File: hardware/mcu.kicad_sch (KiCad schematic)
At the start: 22 parts, among them J6 Micro_SD_Card_Det1, SW24 BOOT, SW8 RST, U1 ESP32-S3-WROOM-1

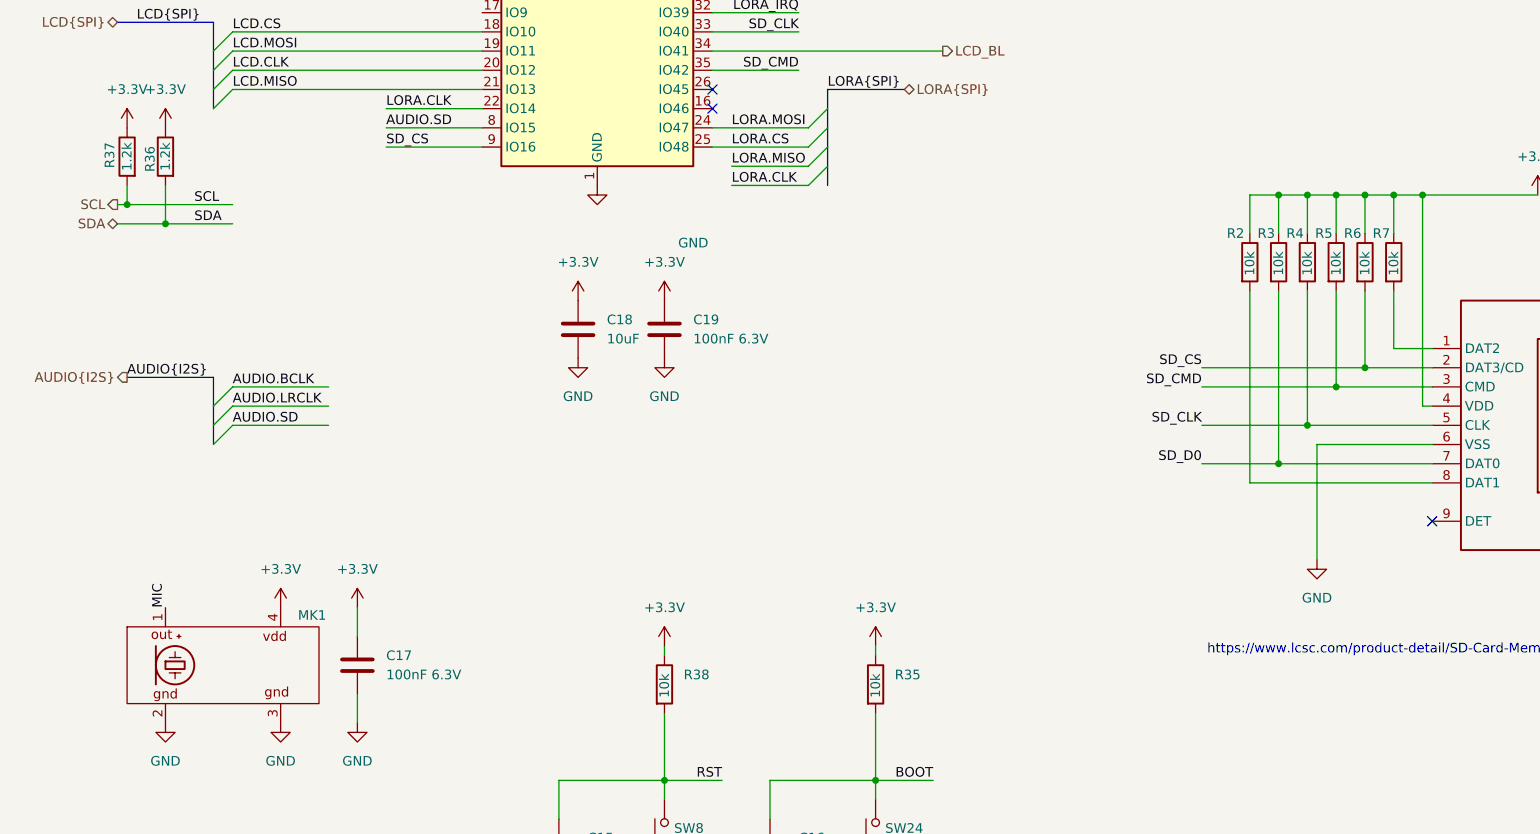
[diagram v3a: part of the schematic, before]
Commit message: Associate all LCSC component
Change sdcard pullup resistor to 47K
Center main schematic
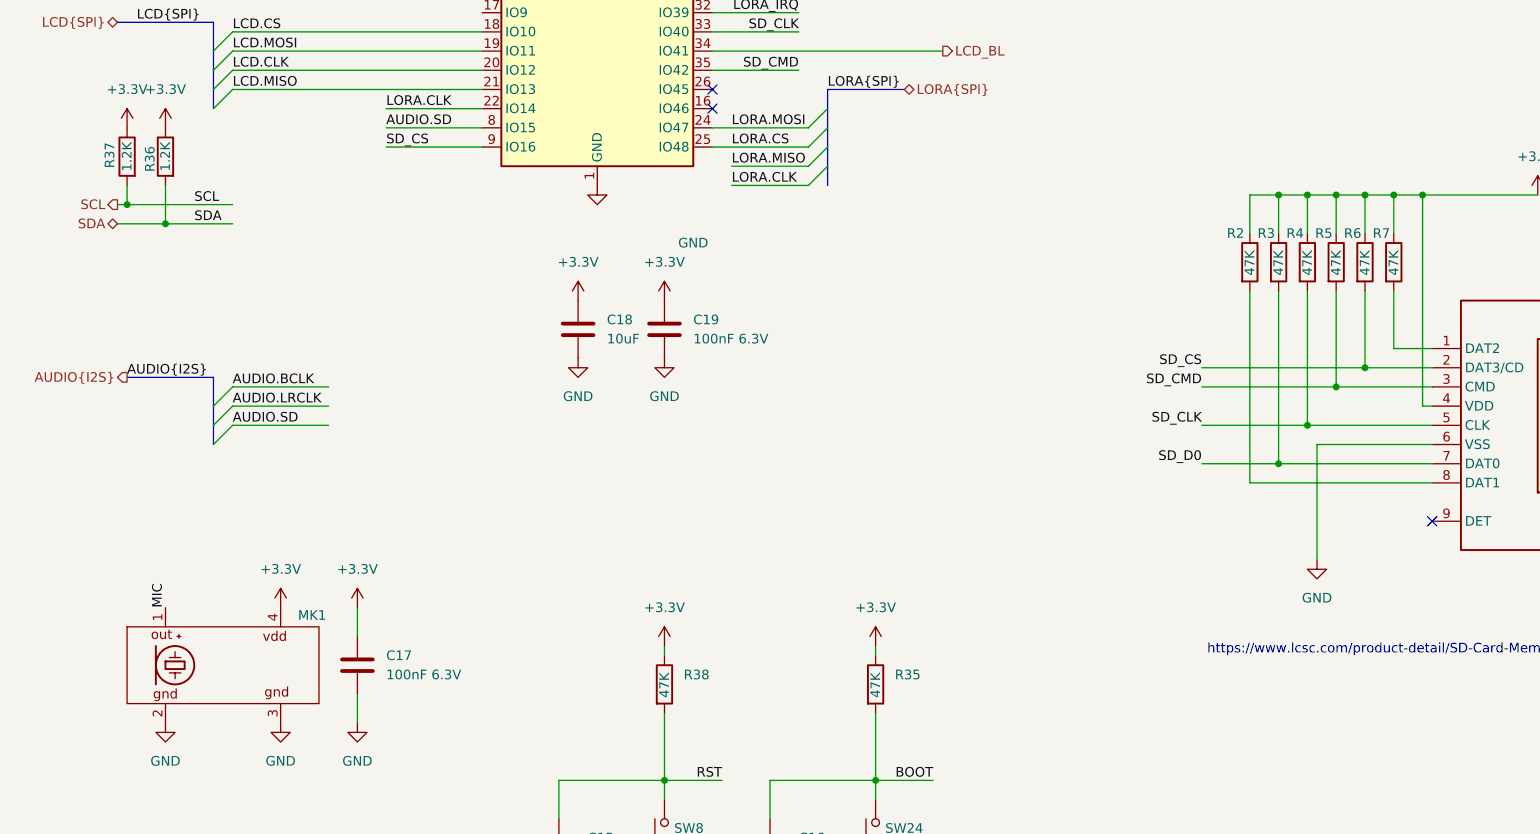
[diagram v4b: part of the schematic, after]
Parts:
- C15, C16, C18: LCSC (none) -> C1691
- R2: value 10k -> 47K; LCSC TODO -> C105579
- R3, R35, R38, R4, R5, R6, R7: value 10k -> 47K; LCSC (none) -> C105579
- R36, R37: value 1.2k -> 1.2K; LCSC (none) -> C114605
- SW24, SW8: LCSC (none) -> C2888430
- U1: LCSC (none) -> C2913201
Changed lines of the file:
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@@
+			)
+		)
+		(property "LCSC" "C2888430"
+			(at 123.19 180.34 0)
+			(effects
+				(font
+					(size 1.27 1.27)
+				)
+				(hide yes)
 			)
 		)
@@
 			)
 		)
-		(property "Value" "10k"
+		(property "Value" "47K"
 			(at 172.72 105.918 90)
 			(effects
@@
 			)
 		)
-		(property "LCSC" "TODO"
+		(property "LCSC" "C105579"
 			(at 172.72 104.14 0)
 			(effects
@@
 			)
 		)
-		(property "Value" "1.2k"
+		(property "Value" "1.2K"
 			(at 29.21 90.17 90)
 			(effects
@@
 			)
 		)
+		(property "LCSC" "C114605"
+			(at 29.21 90.17 0)
+			(effects
+				(font
+					(size 1.27 1.27)
+				)
+				(hide yes)
+			)
+		)
 		(pin "2"
 		)
@@
 			)
 		)
-		(property "Value" "10k"
+		(property "Value" "47K"
 			(at 95.25 161.798 90)
 			(effects
@@
 		)
 		(property "Description" "Resistor"
+			(at 95.25 160.02 0)
+			(effects
+				(font
+					(size 1.27 1.27)
+				)
+				(hide yes)
+			)
+		)
+		(property "LCSC" "C105579"
 			(at 95.25 160.02 0)
 			(effects
@@
 			)
 		)
-		(property "Value" "1.2k"
+		(property "Value" "1.2K"
 			(at 24.13 90.17 90)
 			(effects
@@
 		)
 		(property "Description" "Resistor"
+			(at 24.13 90.17 0)
+			(effects
+				(font
+					(size 1.27 1.27)
+				)
+				(hide yes)
+			)
+		)
+		(property "LCSC" "C114605"
 			(at 24.13 90.17 0)
 			(effects
@@
 			)
 		)
+		(property "LCSC" "C2888430"
+			(at 95.25 180.34 0)
+			(effects
+				(font
+					(size 1.27 1.27)
+				)
+				(hide yes)
+			)
+		)
 		(pin "1"
 		)
@@
 			)
 		)
-		(property "Value" "10k"
+		(property "Value" "47K"
 			(at 176.53 105.918 90)
 			(effects
@@
 			)
 		)
+		(property "LCSC" "C105579"
+			(at 176.53 104.14 0)
+			(effects
+				(font
+					(size 1.27 1.27)
+				)
+				(hide yes)
+			)
+		)
 		(pin "2"
 		)
@@
 			)
 		)
+		(property "LCSC" "C2913201"
+			(at 86.36 66.04 0)
+			(effects
+				(font
+					(size 1.27 1.27)
+				)
+				(hide yes)
+			)
+		)
 		(pin "6"
 		)
@@
 			)
 		)
+		(property "LCSC" "C1691"
+			(at 83.82 113.03 0)
+			(effects
+				(font
+					(size 1.27 1.27)
+				)
+				(hide yes)
+			)
+		)
 		(pin "2"
 		)
@@
 			)
 		)
-		(property "Value" "10k"
+		(property "Value" "47K"
 			(at 191.77 105.918 90)
 			(effects
@@
 			)
 		)
+		(property "LCSC" "C105579"
+			(at 191.77 104.14 0)
+			(effects
+				(font
+					(size 1.27 1.27)
+				)
+				(hide yes)
+			)
+		)
 		(pin "2"
 		)
@@
 			)
 		)
-		(property "Value" "10k"
+		(property "Value" "47K"
 			(at 187.96 105.918 90)
 			(effects
@@
 			)
 		)
+		(property "LCSC" "C105579"
+			(at 187.96 104.14 0)
+			(effects
+				(font
+					(size 1.27 1.27)
+				)
+				(hide yes)
+			)
+		)
 		(pin "2"
 		)
@@
 			)
 		)
+		(property "LCSC" "C1691"
+			(at 109.22 181.61 0)
+			(effects
+				(font
+					(size 1.27 1.27)
+				)
+				(hide yes)
+			)
+		)
 		(pin "2"
 		)
@@
 			)
 		)
-		(property "Value" "10k"
+		(property "Value" "47K"
 			(at 123.19 161.798 90)
 			(effects
@@
 		)
 		(property "Description" "Resistor"
+			(at 123.19 160.02 0)
+			(effects
+				(font
+					(size 1.27 1.27)
+				)
+				(hide yes)
+			)
+		)
+		(property "LCSC" "C105579"
 			(at 123.19 160.02 0)
 			(effects
@@
 			)
 		)
+		(property "LCSC" "C1691"
+			(at 81.28 181.61 0)
+			(effects
+				(font
+					(size 1.27 1.27)
+				)
+				(hide yes)
+			)
+		)
 		(pin "2"
 		)
@@
 			)
 		)
-		(property "Value" "10k"
+		(property "Value" "47K"
 			(at 180.34 105.918 90)
 			(effects
@@
 			)
 		)
+		(property "LCSC" "C105579"
+			(at 180.34 104.14 0)
+			(effects
+				(font
+					(size 1.27 1.27)
+				)
+				(hide yes)
+			)
+		)
 		(pin "2"
 		)
@@
 			)
 		)
-		(property "Value" "10k"
+		(property "Value" "47K"
 			(at 184.15 105.918 90)
 			(effects
@@
 			(at 184.15 104.14 0)
 			(effects
+				(font
+					(size 1.27 1.27)
+				)
+				(hide yes)
+			)
+		)
+		(property "LCSC" "C105579"
+			(at 184.15 104.14 0)
+			(effects

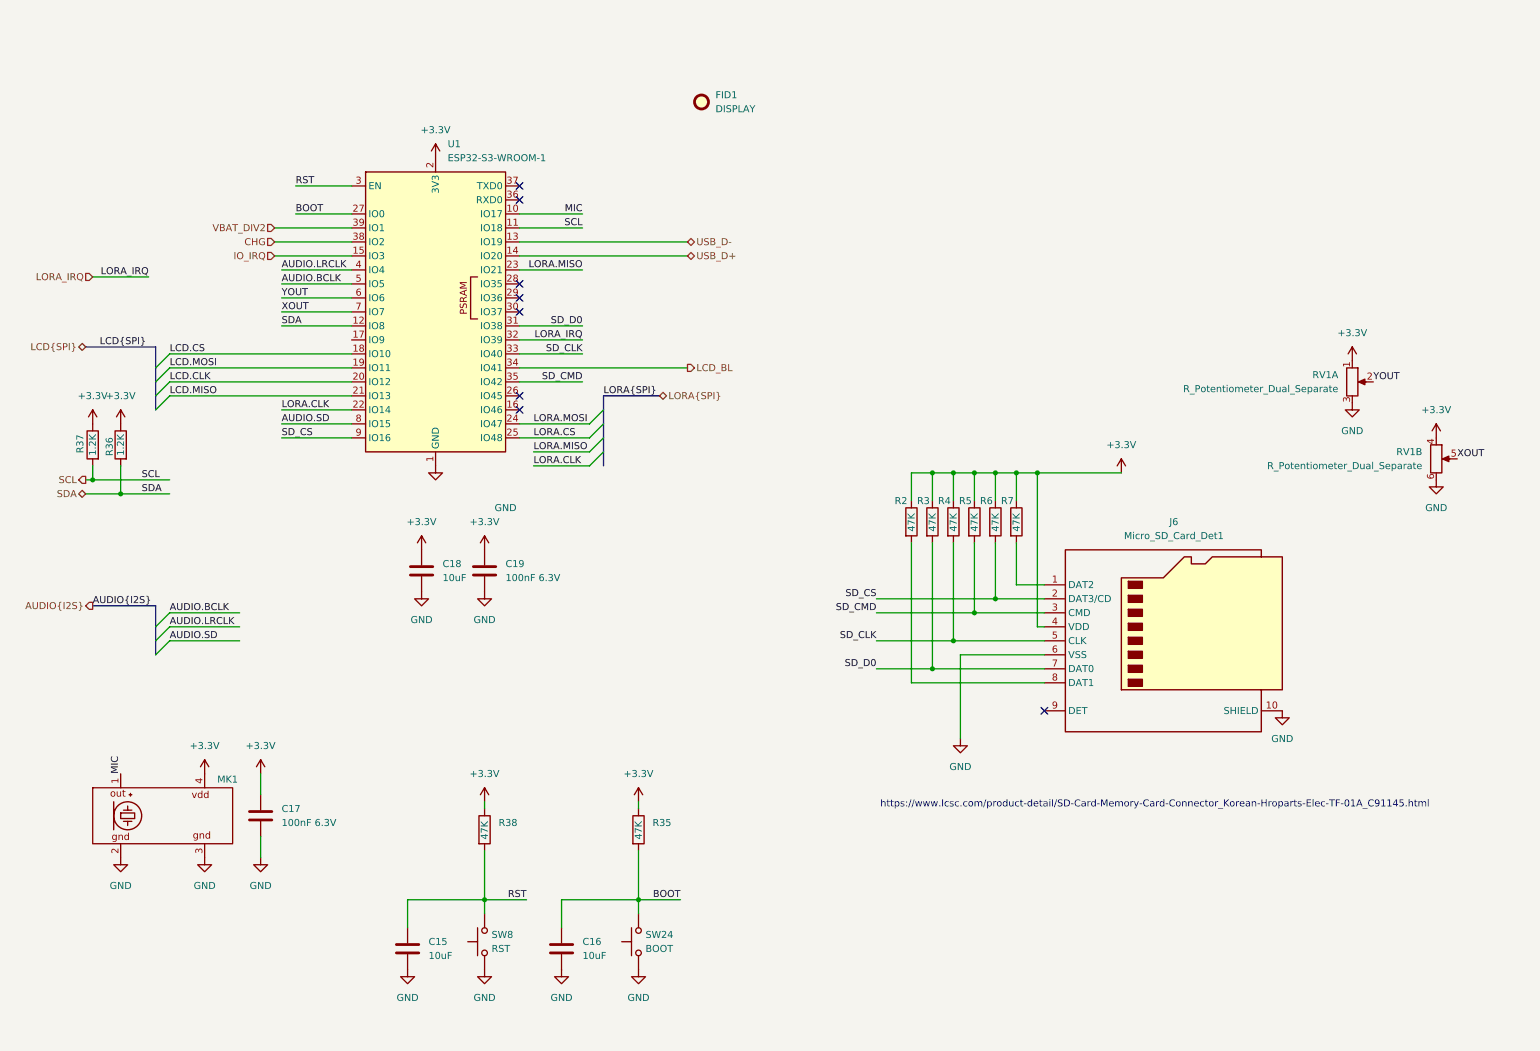
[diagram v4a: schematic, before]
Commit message: Beautified schematic, added I2C addresses
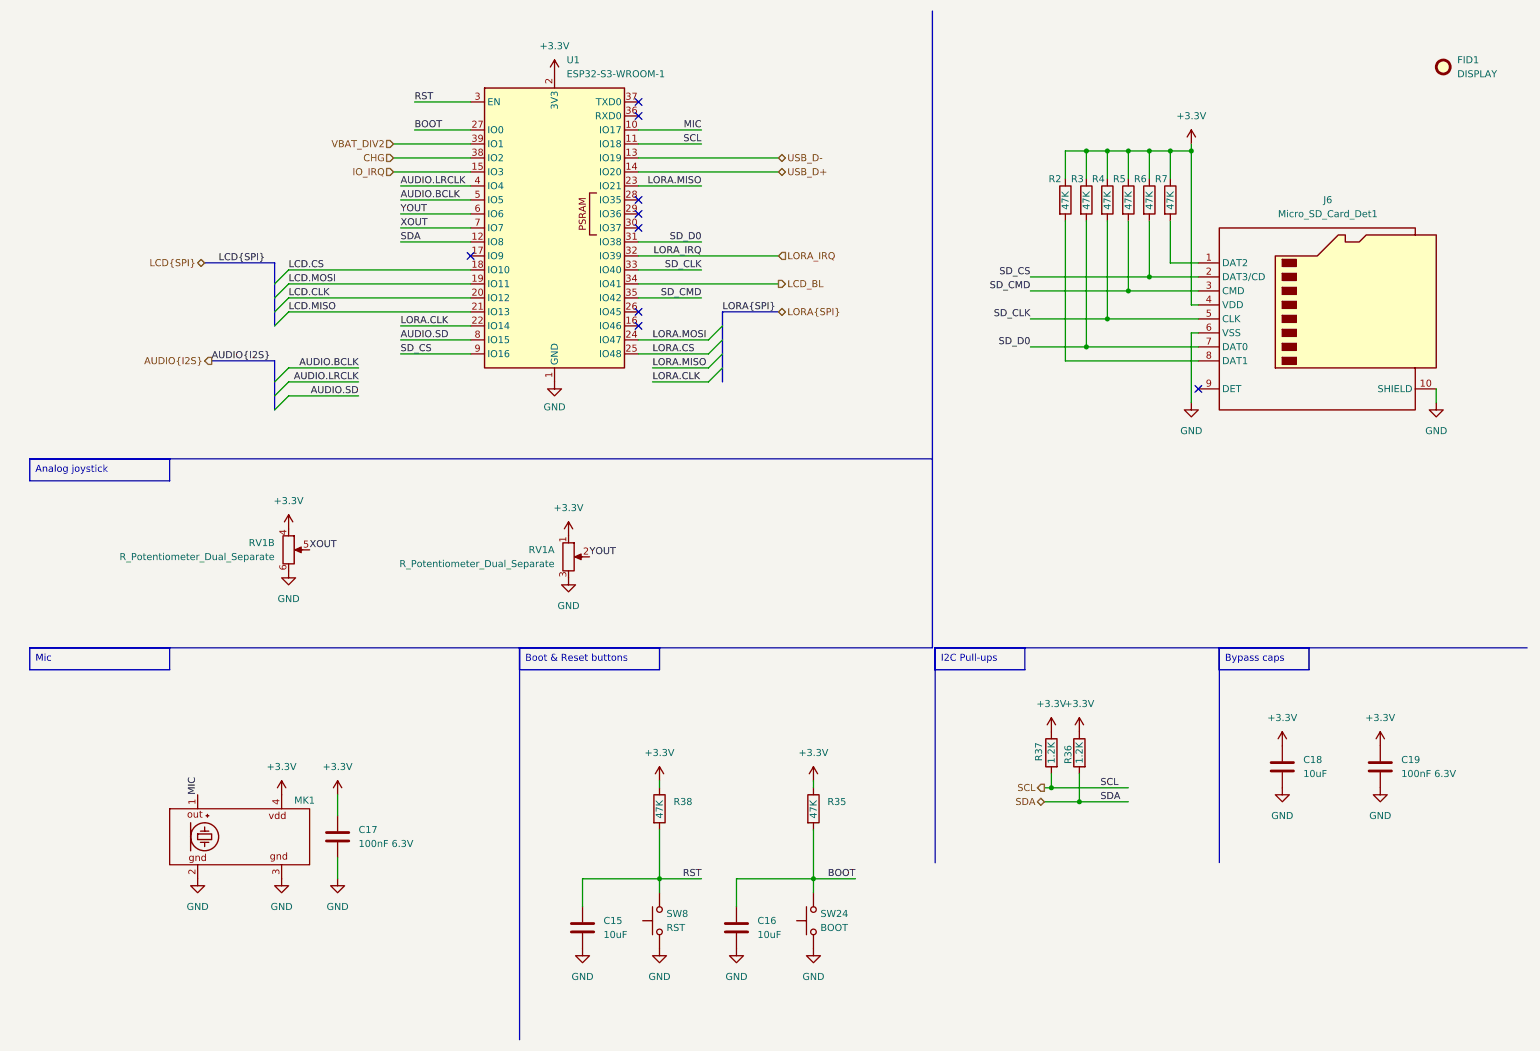
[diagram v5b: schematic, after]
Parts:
- J6: LCSC Link (none) -> https://www.lcsc.com/product-detail/SD-Card-Memory-Card-Con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
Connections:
- no-connect marks 8 -> 9
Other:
- note removed: "https://www.lcsc.com/product-detail/SD-Card-Memory-Card-Connector_Korean-Hroparts-Elec-TF-01A_C91145.html"
- moved on the sheet: C15, C16, C17, C18, C19, FID1, J6, MK1, R2, R3, R35, R36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

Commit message: Fix rotation and position offset of components
Fix lora module rotation
Fix esp32 module position offset
Fix sd card position offset
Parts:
- J6: JLCPCB Position Offset (none) -> 0,5.5
- U1: JLCPCB Position Offset (none) -> 0,-3.65
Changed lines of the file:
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@@
 			)
 		)
+		(property "JLCPCB Position Offset" ""
+			(at 154.94 176.53 0)
+			(effects
+				(font
+					(size 1.27 1.27)
+				)
+				(hide yes)
+			)
+		)
 		(pin "1"
 		)
@@
 			)
 		)
+		(property "JLCPCB Position Offset" ""
+			(at 200.66 45.72 0)
+			(effects
+				(font
+					(size 1.27 1.27)
+				)
+				(hide yes)
+			)
+		)
 		(pin "2"
 		)
@@
 			)
 		)
+		(property "JLCPCB Position Offset" ""
+			(at 203.2 146.05 0)
+			(effects
+				(font
+					(size 1.27 1.27)
+				)
+				(hide yes)
+			)
+		)
 		(pin "2"
 		)
@@
 			)
 		)
+		(property "JLCPCB Position Offset" ""
+			(at 127 156.21 0)
+			(effects
+				(font
+					(size 1.27 1.27)
+				)
+				(hide yes)
+			)
+		)
 		(pin "1"
 		)
@@
 			)
 		)
+		(property "JLCPCB Position Offset" ""
+			(at 198.12 146.05 0)
+			(effects
+				(font
+					(size 1.27 1.27)
+				)
+				(hide yes)
+			)
+		)
 		(pin "2"
 		)
@@
 			)
 		)
+		(property "JLCPCB Position Offset" ""
+			(at 269.24 21.59 0)
+			(effects
+				(font
+					(size 1.27 1.27)
+				)
+				(hide yes)
+			)
+		)
 		(instances
 			(project "badge"
@@
 			)
 		)
+		(property "JLCPCB Position Offset" ""
+			(at 127 176.53 0)
+			(effects
+				(font
+					(size 1.27 1.27)
+				)
+				(hide yes)
+			)
+		)
 		(pin "1"
 		)
@@
 			)
 		)
+		(property "JLCPCB Position Offset" ""
+			(at 204.47 45.72 0)
+			(effects
+				(font
+					(size 1.27 1.27)
+				)
+				(hide yes)
+			)
+		)
 		(pin "2"
 		)
@@
 			)
 		)
+		(property "JLCPCB Position Offset" ""
+			(at 49.53 161.29 0)
+			(effects
+				(font
+					(size 1.27 1.27)
+				)
+				(hide yes)
+			)
+		)
 		(pin "2"
 		)
@@
 			)
 		)
+		(property "JLCPCB Position Offset" "0,-3.65"
+			(at 107.95 50.8 0)
+			(effects
+				(font
+					(size 1.27 1.27)
+				)
+				(hide yes)
+			)
+		)
 		(pin "6"
 		)
@@
 			)
 		)
+		(property "JLCPCB Position Offset" ""
+			(at 240.03 148.59 0)
+			(effects
+				(font
+					(size 1.27 1.27)
+				)
+				(hide yes)
+			)
+		)
 		(pin "2"
 		)
@@
 			)
 		)
+		(property "JLCPCB Position Offset" ""
+			(at 219.71 45.72 0)
+			(effects
+				(font
+					(size 1.27 1.27)
+				)
+				(hide yes)
+			)
+		)
 		(pin "2"
 		)
@@
 			)
 		)
+		(property "JLCPCB Position Offset" ""
+			(at 215.9 45.72 0)
+			(effects
+				(font
+					(size 1.27 1.27)
+				)
+				(hide yes)
+			)
+		)
 		(pin "2"
 		)
@@
 			)
 		)
+		(property "JLCPCB Position Offset" ""
+			(at 140.97 177.8 0)
+			(effects
+				(font
+					(size 1.27 1.27)
+				)
+				(hide yes)
+			)
+		)
 		(pin "2"
 		)
@@
 			)
 		)
+		(property "JLCPCB Position Offset" "0,5.5"
+			(at 247.65 67.31 0)
+			(effects
+				(font
+					(size 1.27 1.27)
+				)
+				(hide yes)
+			)
+		)
 		(pin "6"
 		)
@@
 			)
 		)
+		(property "JLCPCB Position Offset" ""
+			(at 154.94 156.21 0)
+			(effects
+				(font
+					(size 1.27 1.27)
+				)
+				(hide yes)
+			)
+		)
 		(pin "1"
 		)
@@
 			)
 		)
+		(property "JLCPCB Position Offset" ""
+			(at 257.81 148.59 0)
+			(effects
+				(font
+					(size 1.27 1.27)
+				)
+				(hide yes)
+			)
+		)
 		(pin "2"
 		)
@@
 			)
 		)
+		(property "JLCPCB Position Offset" ""
+			(at 113.03 177.8 0)
+			(effects
+				(font
+					(size 1.27 1.27)
+				)
+				(hide yes)
+			)
+		)
 		(pin "2"
 		)
@@
 			)
 		)
+		(property "JLCPCB Position Offset" ""
+			(at 208.28 45.72 0)
+			(effects
+				(font
+					(size 1.27 1.27)
+				)
+				(hide yes)
+			)
+		)
 		(pin "2"
 		)
@@
 			)
 		)
+		(property "JLCPCB Position Offset" ""
+			(at 212.09 45.72 0)
+			(effects
+				(font
+					(size 1.27 1.27)
+				)
+				(hide yes)
+			)
+		)
 		(pin "2"
 		)
@@
 			)
 		)
+		(property "JLCPCB Position Offset" ""
+			(at 110.49 110.49 0)
+			(effects
+				(font
+					(size 1.27 1.27)
+				)
+				(hide yes)
+			)
+		)
 		(pin "2"
 		)
@@
 			)
 		)
+		(property "JLCPCB Position Offset" ""
+			(at 59.69 109.22 0)
+			(effects
+				(font
+					(size 1.27 1.27)
+				)
+				(hide yes)
+			)
+		)
 		(pin "2"
 		)
@@
 			(at 68.58 161.29 0)
 			(effects
+				(font
+					(size 1.27 1.27)
+				)
+				(hide yes)
+			)
+		)
+		(property "JLCPCB Position Offset" ""
+			(at 68.58 161.29 0)
+			(effects

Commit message: add joystick lcsc code, for real
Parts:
- RV1: LCSC (none) -> C17511761
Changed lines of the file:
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@@
+			)
+		)
+		(property "LCSC" "C17511761"
+			(at 110.49 110.49 0)
+			(effects
+				(font
+					(size 1.27 1.27)
+				)
+				(hide yes)
 			)
 		)
@@
 			(at 59.69 109.22 0)
 			(effects
+				(font
+					(size 1.27 1.27)
+				)
+				(hide yes)
+			)
+		)
+		(property "LCSC" "C17511761"
+			(at 59.69 109.22 0)
+			(effects

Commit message: update lcsc codes to use (new?) basic components
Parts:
- C15, C16, C18: LCSC C1691 -> C19702
- R2, R3, R35, R38, R4, R5, R6, R7: LCSC C105579 -> C25819
- R36, R37: LCSC C114605 -> C22765
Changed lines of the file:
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@@
 			)
 		)
-		(property "LCSC" "C105579"
+		(property "LCSC" "C25819"
 			(at 200.66 45.72 0)
 			(effects
@@
 			)
 		)
-		(property "LCSC" "C114605"
+		(property "LCSC" "C22765"
 			(at 203.2 146.05 0)
 			(effects
@@
 			)
 		)
-		(property "LCSC" "C105579"
+		(property "LCSC" "C25819"
 			(at 127 156.21 0)
 			(effects
@@
 			)
 		)
-		(property "LCSC" "C114605"
+		(property "LCSC" "C22765"
 			(at 198.12 146.05 0)
 			(effects
@@
 			)
 		)
-		(property "LCSC" "C105579"
+		(property "LCSC" "C25819"
 			(at 204.47 45.72 0)
 			(effects
@@
 			)
 		)
-		(property "LCSC" "C1691"
+		(property "LCSC" "C19702"
 			(at 240.03 148.59 0)
 			(effects
@@
 			)
 		)
-		(property "LCSC" "C105579"
+		(property "LCSC" "C25819"
 			(at 219.71 45.72 0)
 			(effects
@@
 			)
 		)
-		(property "LCSC" "C105579"
+		(property "LCSC" "C25819"
 			(at 215.9 45.72 0)
 			(effects
@@
 			)
 		)
-		(property "LCSC" "C1691"
+		(property "LCSC" "C19702"
 			(at 140.97 177.8 0)
 			(effects
@@
 			)
 		)
-		(property "LCSC" "C105579"
+		(property "LCSC" "C25819"
 			(at 154.94 156.21 0)
 			(effects
@@
 			)
 		)
-		(property "LCSC" "C1691"
+		(property "LCSC" "C19702"
 			(at 113.03 177.8 0)
 			(effects
@@
 			)
 		)
-		(property "LCSC" "C105579"
+		(property "LCSC" "C25819"
 			(at 208.28 45.72 0)
 			(effects
@@
 			)
 		)
-		(property "LCSC" "C105579"
+		(property "LCSC" "C25819"
 			(at 212.09 45.72 0)
 			(effects
